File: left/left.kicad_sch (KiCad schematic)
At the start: 18 parts, among them J1 USB_C_Receptacle_IN, J2 USB_C_Receptacle_OUT, SW1 SW_Push, SW2 SW_SPDT, U1 STM32G0B1CBTx, U2 SRV05-4, U3 XC6206P332MR

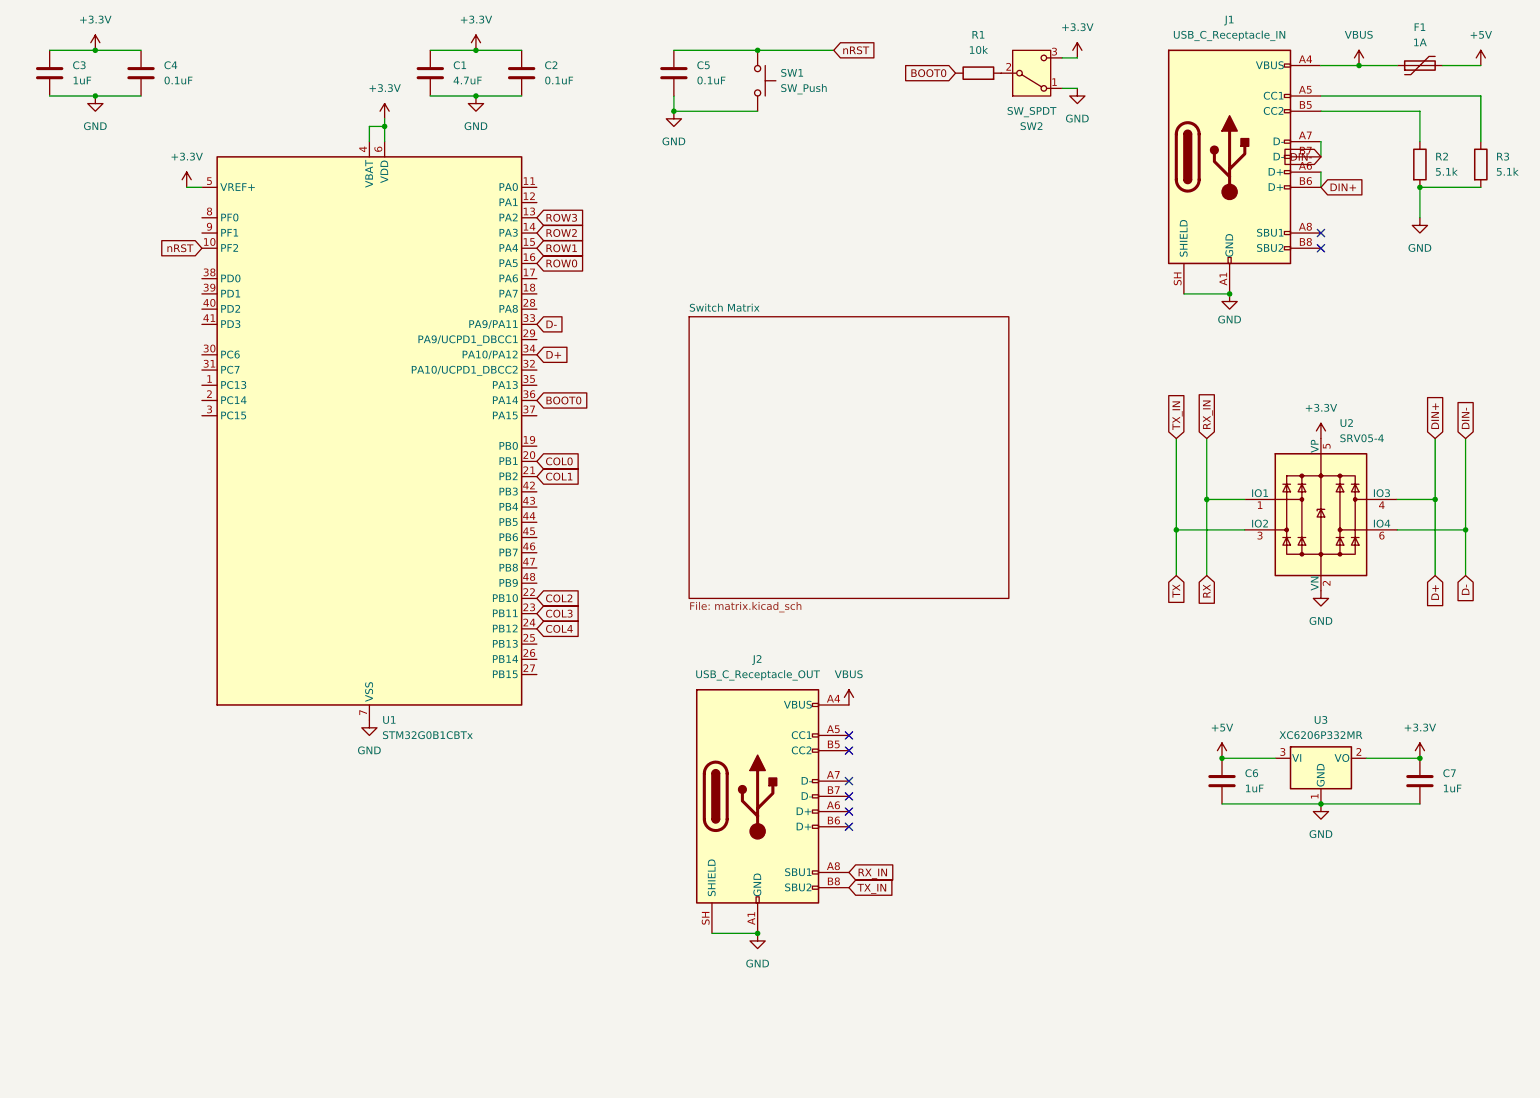
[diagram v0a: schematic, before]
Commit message: redesigned pcb
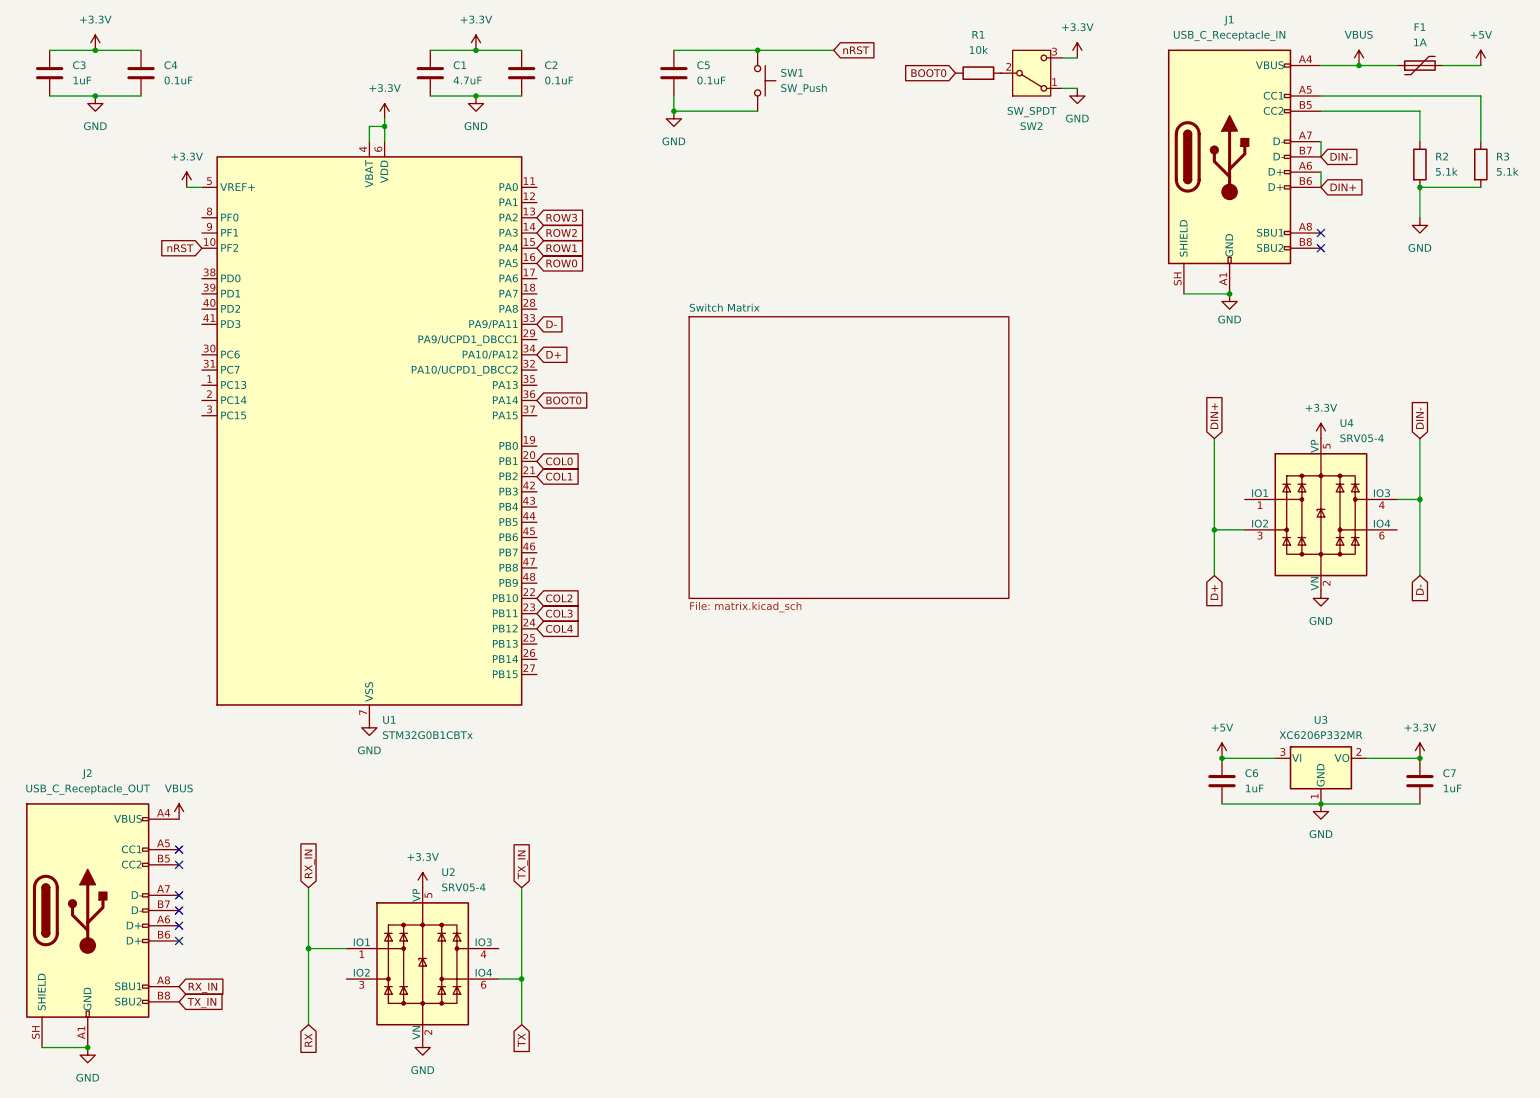
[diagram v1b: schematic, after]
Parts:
- added U4: SRV05-4, Package_TO_SOT_SMD:SOT-23-6, symbol Power_Protection:SRV05-4
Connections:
- net +3.3V: now also U4.5 (VP)
- net D+: now also U4.3 (IO2); no longer U2.4 (IO3)
- net D-: now also U4.4 (IO3); no longer U2.6 (IO4)
- net GND: now also U4.2 (VN)
- net TX: now also U2.6 (IO4); no longer U2.3 (IO2)
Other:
- moved on the sheet: J2, U2

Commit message: should be done?
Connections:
- net COL0: now also U1.17 (PA6); no longer U1.20 (PB1)
- net COL1: now also U1.16 (PA5); no longer U1.21 (PB2)
- net COL2: now also U1.15 (PA4); no longer U1.22 (PB10)
- net COL3: now also U1.14 (PA3); no longer U1.23 (PB11)
- net COL4: now also U1.13 (PA2); no longer U1.24 (PB12)
- net ROW0: now also U1.21 (PB2); no longer U1.16 (PA5)
- net ROW1: now also U1.22 (PB10); no longer U1.15 (PA4)
- net ROW2: now also U1.23 (PB11); no longer U1.14 (PA3)
- net ROW3: now also U1.24 (PB12); no longer U1.13 (PA2)
- net RX: now also U1.26 (PB14)
- net TX: now also U1.25 (PB13)

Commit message: fixed schematics
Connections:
- net ROW0: now also U1.18 (PA7); no longer U1.21 (PB2)
- net ROW1: now also U1.19 (PB0); no longer U1.22 (PB10)
- net ROW2: now also U1.20 (PB1); no longer U1.23 (PB11)
- net ROW3: now also U1.21 (PB2); no longer U1.24 (PB12)
- net RX: now also U1.23 (PB11); no longer U1.26 (PB14)
- net TX: now also U1.22 (PB10); no longer U1.25 (PB13)
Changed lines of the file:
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@@
 	(global_label "TX"
 		(shape input)
-		(at 111.76 120.65 0)
-		(fields_autoplaced yes)
-		(effects
-			(font
-				(size 1.27 1.27)
-			)
-			(justify left)
-		)
-		(property "Intersheetrefs" "${INTERSHEET_REFS}"
-			(at 116.9223 120.65 0)
+		(at 111.76 113.03 0)
+		(fields_autoplaced yes)
+		(effects
+			(font
+				(size 1.27 1.27)
+			)
+			(justify left)
+		)
+		(property "Intersheetrefs" "${INTERSHEET_REFS}"
+			(at 116.9223 113.03 0)
 			(hide yes)
 			(show_name no)
@@
 	(global_label "RX"
 		(shape input)
-		(at 111.76 123.19 0)
-		(fields_autoplaced yes)
-		(effects
-			(font
-				(size 1.27 1.27)
-			)
-			(justify left)
-		)
-		(property "Intersheetrefs" "${INTERSHEET_REFS}"
-			(at 117.2247 123.19 0)
+		(at 111.76 115.57 0)
+		(fields_autoplaced yes)
+		(effects
+			(font
+				(size 1.27 1.27)
+			)
+			(justify left)
+		)
+		(property "Intersheetrefs" "${INTERSHEET_REFS}"
+			(at 117.2247 115.57 0)
 			(hide yes)
 			(show_name no)
@@
 	(global_label "ROW1"
 		(shape input)
-		(at 111.76 113.03 0)
-		(fields_autoplaced yes)
-		(effects
-			(font
-				(size 1.27 1.27)
-			)
-			(justify left)
-		)
-		(property "Intersheetrefs" "${INTERSHEET_REFS}"
-			(at 120.0066 113.03 0)
+		(at 111.76 87.63 0)
+		(fields_autoplaced yes)
+		(effects
+			(font
+				(size 1.27 1.27)
+			)
+			(justify left)
+		)
+		(property "Intersheetrefs" "${INTERSHEET_REFS}"
+			(at 120.0066 87.63 0)
 			(hide yes)
 			(show_name no)
@@
 	(global_label "ROW3"
 		(shape input)
-		(at 111.76 118.11 0)
-		(fields_autoplaced yes)
-		(effects
-			(font
-				(size 1.27 1.27)
-			)
-			(justify left)
-		)
-		(property "Intersheetrefs" "${INTERSHEET_REFS}"
-			(at 120.0066 118.11 0)
+		(at 111.76 92.71 0)
+		(fields_autoplaced yes)
+		(effects
+			(font
+				(size 1.27 1.27)
+			)
+			(justify left)
+		)
+		(property "Intersheetrefs" "${INTERSHEET_REFS}"
+			(at 120.0066 92.71 0)
 			(hide yes)
 			(show_name no)
@@
 	(global_label "ROW0"
 		(shape input)
-		(at 111.76 92.71 0)
-		(fields_autoplaced yes)
-		(effects
-			(font
-				(size 1.27 1.27)
-			)
-			(justify left)
-		)
-		(property "Intersheetrefs" "${INTERSHEET_REFS}"
-			(at 120.0066 92.71 0)
+		(at 111.76 62.23 0)
+		(fields_autoplaced yes)
+		(effects
+			(font
+				(size 1.27 1.27)
+			)
+			(justify left)
+		)
+		(property "Intersheetrefs" "${INTERSHEET_REFS}"
+			(at 120.0066 62.23 0)
 			(hide yes)
 			(show_name no)
@@
 	(global_label "ROW2"
 		(shape input)
-		(at 111.76 115.57 0)
-		(fields_autoplaced yes)
-		(effects
-			(font
-				(size 1.27 1.27)
-			)
-			(justify left)
-		)
-		(property "Intersheetrefs" "${INTERSHEET_REFS}"
-			(at 120.0066 115.57 0)
-			(hide yes)
-			(show_name no)
+		(at 111.76 90.17 0)
+		(fields_autoplaced yes)
+		(effects
+			(font
+				(size 1.27 1.27)
+			)
+			(justify left)
+		)
+		(property "Intersheetrefs" "${INTERSHEET_REFS}"
+			(at 120.0066 90.17 0)
+			(hide yes)
+			(show_name no)

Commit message: v3 for the right side
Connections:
- net RX: now also J2.A7 (D-), J2.B7 (D-), U1.48 (PB9); no longer J2.A8 (SBU1), U1.23 (PB11)
- net TX: now also J2.A6 (D+), J2.B6 (D+), U1.47 (PB8); no longer J2.B8 (SBU2), U1.22 (PB10)
- no-connect marks 8 -> 6
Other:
- moved on the sheet: U2
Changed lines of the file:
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@@
 	(paper "A4")
 	(junction
-		(at 73.66 171.45)
+		(at 113.03 170.18)
 		(diameter 0)
 		(color 0 0 0 0)
@@
 	)
 	(junction
-		(at 109.22 176.53)
+		(at 148.59 175.26)
 		(diameter 0)
 		(color 0 0 0 0)
@@
 	)
 	(no_connect
-		(at 52.07 165.1)
-	)
-	(no_connect
-		(at 52.07 162.56)
-	)
-	(no_connect
-		(at 52.07 170.18)
+		(at 52.07 180.34)
 	)
 	(no_connect
@@
 	)
 	(no_connect
-		(at 52.07 167.64)
+		(at 52.07 177.8)
 	)
 	(no_connect
@@
 	(wire
 		(pts
+			(xy 52.07 167.64) (xy 52.07 170.18)
+		)
+		(stroke
+			(width 0)
+			(type default)
+		)
+	)
+	(wire
+		(pts
 			(xy 101.6 21.59) (xy 109.22 21.59)
 		)
@@
 	(wire
 		(pts
-			(xy 73.66 171.45) (xy 80.01 171.45)
+			(xy 113.03 170.18) (xy 119.38 170.18)
 		)
 		(stroke
@@
 	(wire
 		(pts
-			(xy 73.66 171.45) (xy 73.66 184.15)
+			(xy 113.03 170.18) (xy 113.03 182.88)
 		)
 		(stroke
@@
 	(wire
 		(pts
-			(xy 109.22 161.29) (xy 109.22 176.53)
+			(xy 148.59 160.02) (xy 148.59 175.26)
 		)
 		(stroke
@@
 	(wire
 		(pts
-			(xy 105.41 176.53) (xy 109.22 176.53)
+			(xy 144.78 175.26) (xy 148.59 175.26)
 		)
 		(stroke
@@
 	(wire
 		(pts
-			(xy 73.66 161.29) (xy 73.66 171.45)
+			(xy 52.07 162.56) (xy 52.07 165.1)
+		)
+		(stroke
+			(width 0)
+			(type default)
+		)
+	)
+	(wire
+		(pts
+			(xy 113.03 160.02) (xy 113.03 170.18)
 		)
 		(stroke
@@
 	(wire
 		(pts
-			(xy 109.22 176.53) (xy 109.22 184.15)
+			(xy 148.59 175.26) (xy 148.59 182.88)
 		)
 		(stroke
@@
 	(global_label "RX_IN"
 		(shape input)
-		(at 73.66 161.29 90)
+		(at 113.03 160.02 90)
 		(fields_autoplaced yes)
 		(effects
@@
 		)
 		(property "Intersheetrefs" "${INTERSHEET_REFS}"
-			(at 73.66 152.9224 90)
+			(at 113.03 151.6524 90)
 			(hide yes)
 			(show_name no)
@@
 	(global_label "TX"
 		(shape input)
-		(at 111.76 113.03 0)
+		(at 111.76 107.95 0)
 		(fields_autoplaced yes)
 		(effects
@@
 		)
 		(property "Intersheetrefs" "${INTERSHEET_REFS}"
-			(at 116.9223 113.03 0)
+			(at 116.9223 107.95 0)
 			(hide yes)
 			(show_name no)
@@
 	(global_label "RX"
 		(shape input)
-		(at 111.76 115.57 0)
+		(at 111.76 110.49 0)
 		(fields_autoplaced yes)
 		(effects
@@
 		)
 		(property "Intersheetrefs" "${INTERSHEET_REFS}"
-			(at 117.2247 115.57 0)
+			(at 117.2247 110.49 0)
 			(hide yes)
 			(show_name no)
@@
 	(global_label "TX_IN"
 		(shape input)
-		(at 109.22 161.29 90)
+		(at 148.59 160.02 90)
 		(fields_autoplaced yes)
 		(effects
@@
 		)
 		(property "Intersheetrefs" "${INTERSHEET_REFS}"
-			(at 109.22 153.2248 90)
+			(at 148.59 151.9548 90)
 			(hide yes)
 			(show_name no)
@@
 	(global_label "TX_IN"
 		(shape input)
-		(at 52.07 180.34 0)
+		(at 52.07 170.18 0)
 		(fields_autoplaced yes)
 		(effects
@@
 		)
 		(property "Intersheetrefs" "${INTERSHEET_REFS}"
-			(at 60.1352 180.34 0)
+			(at 60.1352 170.18 0)
 			(hide yes)
 			(show_name no)
@@
 	(global_label "RX_IN"
 		(shape input)
-		(at 52.07 177.8 0)
+		(at 52.07 165.1 0)
 		(fields_autoplaced yes)
 		(effects
@@
 		)
 		(property "Intersheetrefs" "${INTERSHEET_REFS}"
-			(at 60.4376 177.8 0)
+			(at 60.4376 165.1 0)
 			(hide yes)
 			(show_name no)
@@
 	(global_label "TX"
 		(shape input)
-		(at 109.22 184.15 270)
+		(at 148.59 182.88 270)
 		(fields_autoplaced yes)
 		(effects
@@
 		)
 		(property "Intersheetrefs" "${INTERSHEET_REFS}"
-			(at 109.22 189.3123 90)
+			(at 148.59 188.0423 90)
 			(hide yes)
 			(show_name no)
@@
 	(global_label "RX"
 		(shape input)
-		(at 73.66 184.15 270)
+		(at 113.03 182.88 270)
 		(fields_autoplaced yes)
 		(effects
@@
 		)
 		(property "Intersheetrefs" "${INTERSHEET_REFS}"
-			(at 73.66 189.6147 90)
+			(at 113.03 188.3447 90)
 			(hide yes)
 			(show_name no)
@@
 	(symbol
 		(lib_id "power:GND")
-		(at 92.71 186.69 0)
+		(at 132.08 185.42 0)
 		(unit 1)
 		(body_style 1)
@@
 		(fields_autoplaced yes)
 		(property "Reference" "#PWR016"
-			(at 92.71 193.04 0)
+			(at 132.08 191.77 0)
 			(hide yes)
 			(show_name no)
@@
 		)
 		(property "Value" "GND"
-			(at 92.71 191.77 0)
+			(at 132.08 190.5 0)
 			(show_name no)
 			(do_not_autoplace no)
@@
 		)
 		(property "Footprint" ""
-			(at 92.71 186.69 0)
+			(at 132.08 185.42 0)
 			(hide yes)
 			(show_name no)
@@
 		)
 		(property "Datasheet" ""
-			(at 92.71 186.69 0)
+			(at 132.08 185.42 0)
 			(hide yes)
 			(show_name no)
@@
 		)
 		(property "Description" "Power symbol creates a global label with name \"GND\" , ground"
-			(at 92.71 186.69 0)
+			(at 132.08 185.42 0)
 			(hide yes)
 			(show_name no)
@@
 	(symbol
 		(lib_id "power:+3.3V")
-		(at 92.71 161.29 0)
+		(at 132.08 160.02 0)
 		(unit 1)
 		(body_style 1)
@@
 		(fields_autoplaced yes)
 		(property "Reference" "#PWR015"
-			(at 92.71 165.1 0)
+			(at 132.08 163.83 0)
 			(hide yes)
 			(show_name no)
@@
 		)
 		(property "Value" "+3.3V"
-			(at 92.71 156.21 0)
+			(at 132.08 154.94 0)
 			(show_name no)
 			(do_not_autoplace no)
@@
 		)
 		(property "Footprint" ""
-			(at 92.71 161.29 0)
+			(at 132.08 160.02 0)
 			(hide yes)
 			(show_name no)
@@
 		)
 		(property "Datasheet" ""
-			(at 92.71 161.29 0)
+			(at 132.08 160.02 0)
 			(hide yes)
 			(show_name no)
@@
 		)
 		(property "Description" "Power symbol creates a global label with name \"+3.3V\""
-			(at 92.71 161.29 0)
+			(at 132.08 160.02 0)
 			(hide yes)
 			(show_name no)
@@
 	(symbol
 		(lib_id "Power_Protection:SRV05-4")
-		(at 92.71 173.99 0)
+		(at 132.08 172.72 0)
 		(unit 1)
 		(body_style 1)
@@
 		(fields_autoplaced yes)
 		(property "Reference" "U2"
-			(at 95.8281 158.75 0)
+			(at 135.1981 157.48 0)
 			(show_name no)
 			(do_not_autoplace no)
@@
 		)
 		(property "Value" "SRV05-4"
-			(at 95.8281 161.29 0)
+			(at 135.1981 160.02 0)
 			(show_name no)
 			(do_not_autoplace no)
@@
 		)
 		(property "Footprint" "Package_TO_SOT_SMD:SOT-23-6"
-			(at 110.49 185.42 0)
+			(at 149.86 184.15 0)
 			(hide yes)
 			(show_name no)
@@
 		)
 		(property "Datasheet" "http://www.onsemi.com/pub/Collateral/SRV05-4-D.PDF"
-			(at 92.71 173.99 0)
+			(at 132.08 172.72 0)
 			(hide yes)
 			(show_name no)
@@
 		)
 		(property "Description" "ESD Protection Diodes with Low Clamping Voltage, SOT-23-6"
-			(at 92.71 173.99 0)
+			(at 132.08 172.72 0)
 			(hide yes)
 			(show_name no)

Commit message: v3 for left
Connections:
- net COL0: now also U1.23 (PB11); no longer U1.17 (PA6)
- net COL1: now also U1.22 (PB10); no longer U1.16 (PA5)
- net COL2: now also U1.39 (PD1); no longer U1.15 (PA4)
- net COL3: now also U1.38 (PD0); no longer U1.14 (PA3)
- net COL4: now also U1.37 (PA15); no longer U1.13 (PA2)
- net ROW0: now also U1.46 (PB7); no longer U1.18 (PA7)
- net ROW1: now also U1.47 (PB8); no longer U1.19 (PB0)
- net ROW2: now also U1.48 (PB9); no longer U1.20 (PB1)
- net ROW3: now also U1.24 (PB12); no longer U1.21 (PB2)
- net RX: now also U1.19 (PB0), U2.4 (IO3), U2.6 (IO4); no longer U1.48 (PB9), U2.1 (IO1)
- net TX: now also U1.21 (PB2), U2.1 (IO1), U2.3 (IO2); no longer U1.47 (PB8), U2.6 (IO4)
